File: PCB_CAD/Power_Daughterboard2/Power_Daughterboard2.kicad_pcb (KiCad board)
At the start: 2 copper layers, 65 x 60 mm, 7 parts

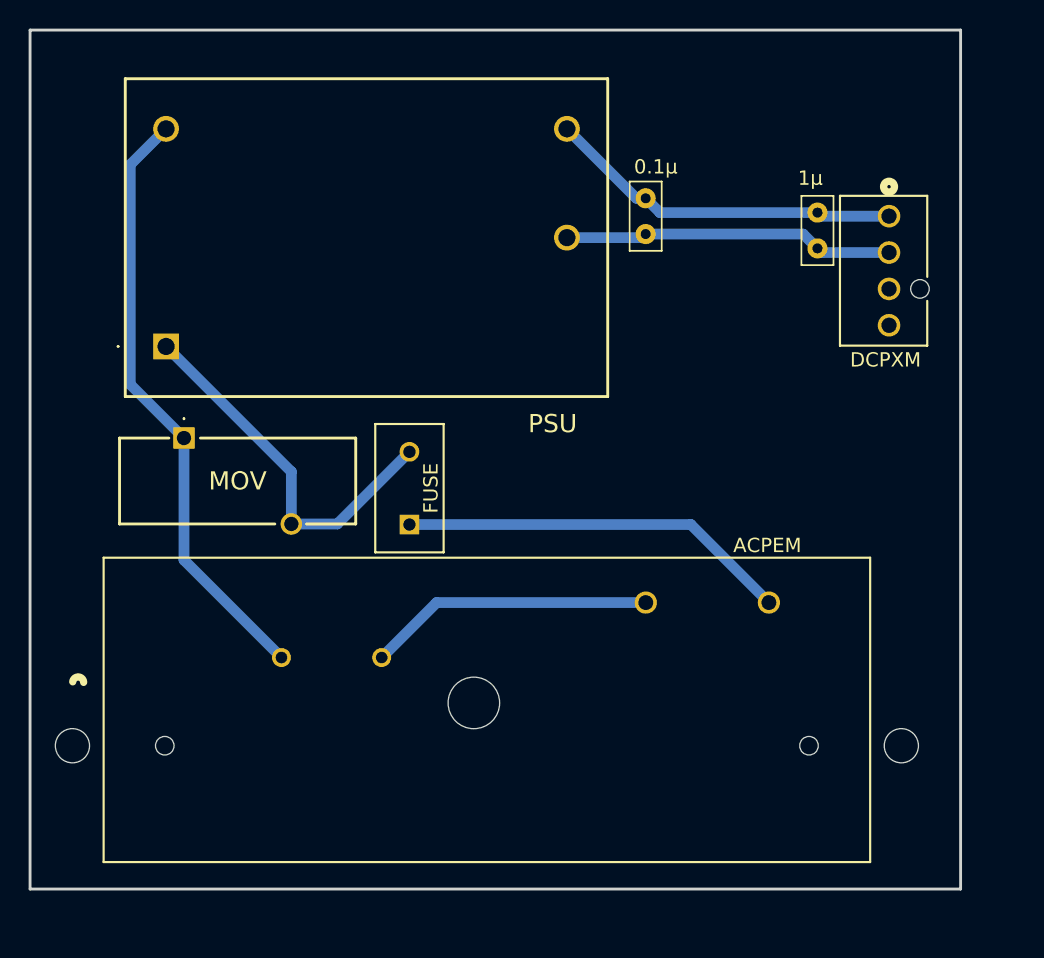
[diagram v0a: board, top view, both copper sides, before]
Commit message: board work, SWD and boot switches, user IO block
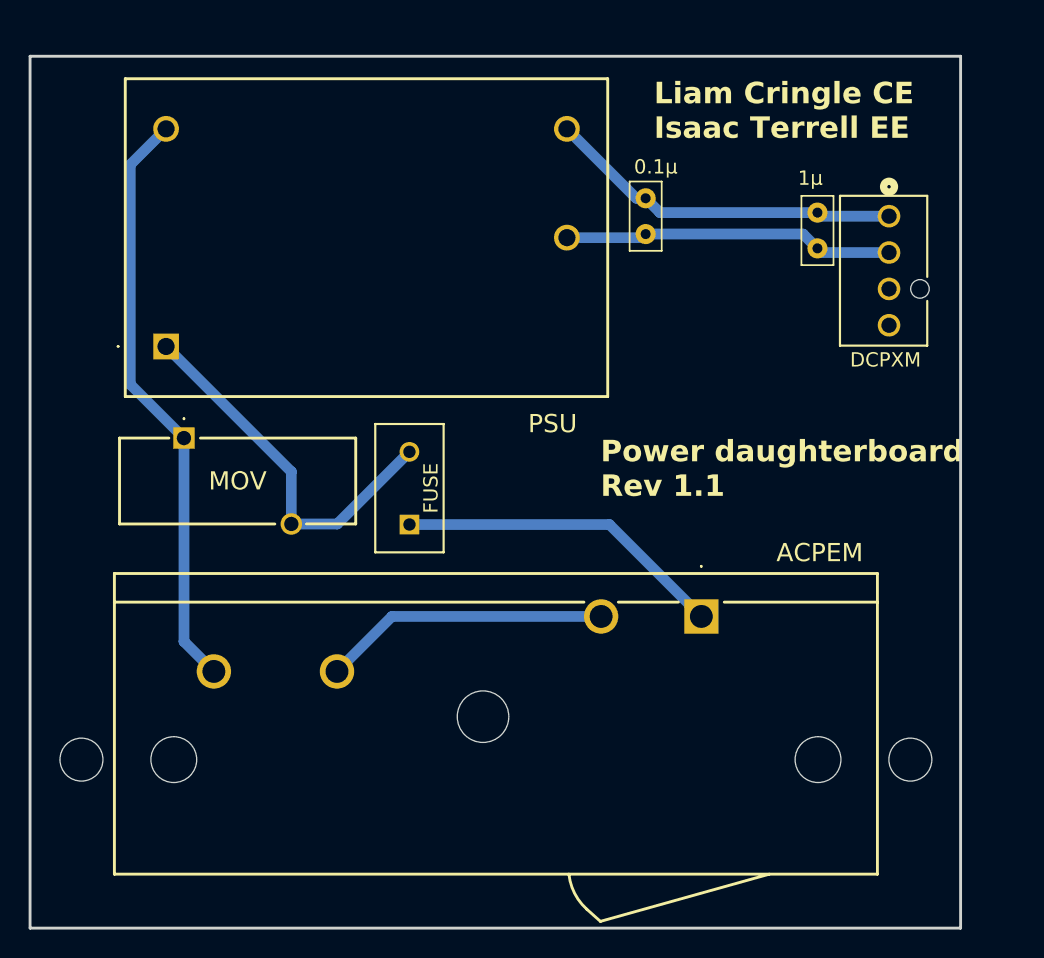
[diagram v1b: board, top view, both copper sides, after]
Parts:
- removed the ACPEM at (122.1, 113.3)
- added ACPEM: CMF2113112, CustomModels:CMF2113112, F.Cu at (151.4, 110.5)
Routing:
- net Net-(FUSE1-Pad1): track 27.4 -> 23.0 mm
- net Net-(PSU1-AC2): track 42.3 -> 41.4 mm
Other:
- board size 65 x 60 mm -> 65 x 60.9 mm
- board text added: "Liam Cringle CE Isaac Terrell EE"
- board text added: "Power daughterboard Rev 1.1"
- board text removed: "Liam Cringle CE Isaac Terrell EE Power daughterboard"
